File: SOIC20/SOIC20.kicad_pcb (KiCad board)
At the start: 2 copper layers, 20.6 x 25.7 mm, 8 parts, among them J1 Conn_01x10, J2 Conn_02x10_Counter_Clockwise, J3 Conn_02x10_Counter_Clockwise, J4 Conn_02x10_Counter_Clockwise, J5 Conn_01x10

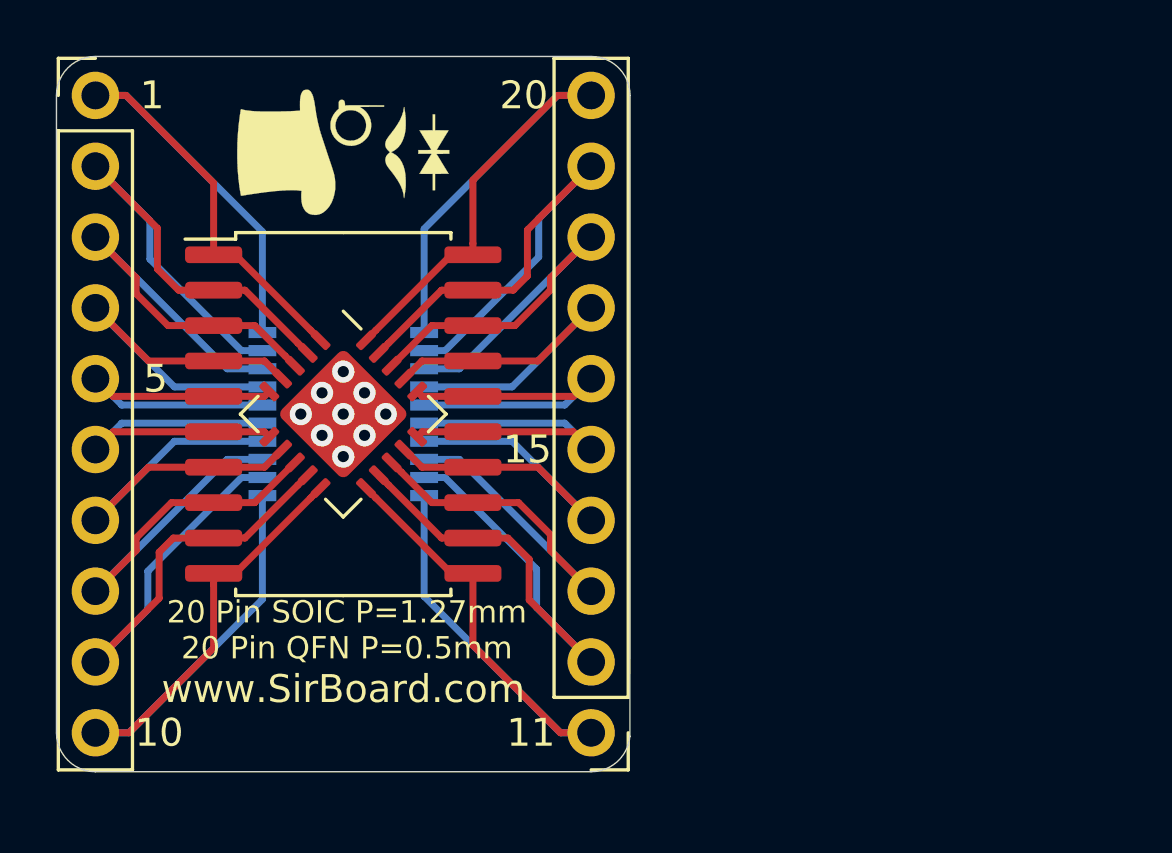
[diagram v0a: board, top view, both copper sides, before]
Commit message: Silkscreens and sizes updated
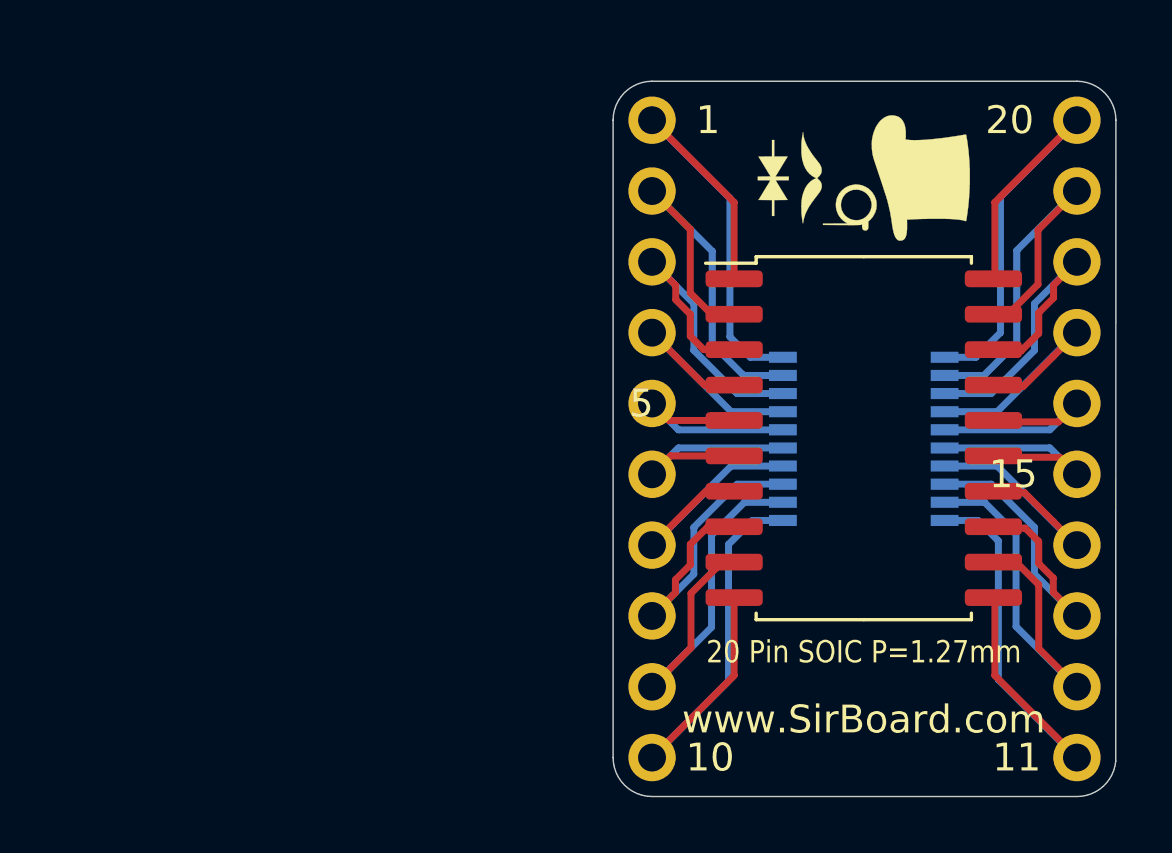
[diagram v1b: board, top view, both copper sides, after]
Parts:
- removed J3: Conn_02x10_Counter_Clockwise, Package_DFN_QFN:QFN-20-1EP_5x5mm_P0.65mm_EP3.35x3.35mm
- moved J1 20.0 mm to (154.6, 105.0)
- moved G*** 18.7 mm to (162.2, 107.1), turned to 270 degrees
- moved G*** 18.7 mm to (162.2, 124.9)
- moved J4 18.7 mm to (162.2, 116.5)
- moved G*** 18.7 mm to (162.2, 109.2)
- moved J2 18.7 mm to (162.2, 116.4)
- moved J5 17.4 mm to (169.8, 127.9)
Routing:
- net Net-(J2-Pad20): track 25.0 -> 18.0 mm
- net Net-(J1-Pad10): track 25.0 -> 18.0 mm
- net Net-(J2-Pad11): track 24.9 -> 18.0 mm
- net Net-(J1-Pad1): track 24.9 -> 18.0 mm
- net Net-(J1-Pad9): track 20.9 -> 15.3 mm
- net Net-(J2-Pad19): track 20.9 -> 15.3 mm
- net Net-(J1-Pad4): track 14.9 -> 9.59 mm
- net Net-(J2-Pad14): track 14.9 -> 9.59 mm
- net Net-(J2-Pad17): track 14.9 -> 9.61 mm
- net Net-(J1-Pad7): track 14.9 -> 9.61 mm
- net Net-(J1-Pad2): track 20.8 -> 15.5 mm
- net Net-(J2-Pad12): track 20.8 -> 15.5 mm
- net Net-(J2-Pad13): track 17.4 -> 12.6 mm
- net Net-(J1-Pad3): track 17.4 -> 12.6 mm
- net Net-(J1-Pad8): track 17.3 -> 12.6 mm
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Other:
- board size 20.6 x 25.7 mm -> 18 x 25.7 mm
- board text added: "20 Pin SOIC P=1.27mm"
- board text removed: "20 Pin SOIC P=1.27mm 20 Pin QFN P=0.5mm"

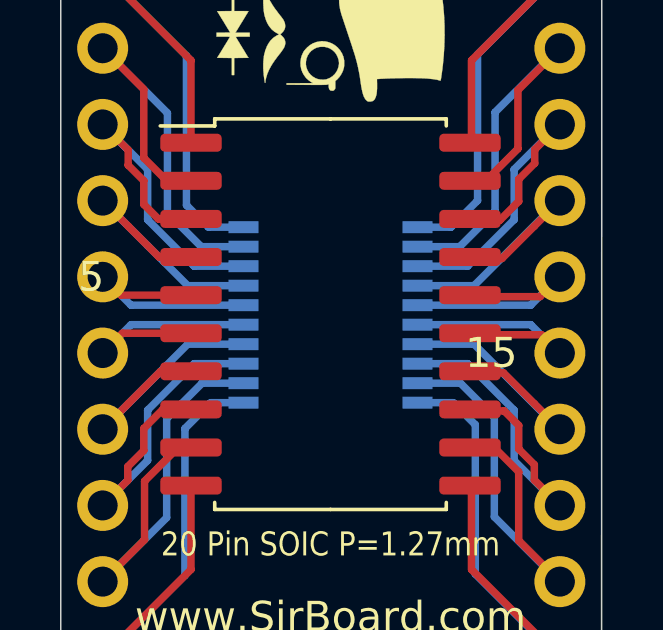
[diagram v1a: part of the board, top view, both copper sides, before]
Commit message: Dimensions Added And TQFP64 Added
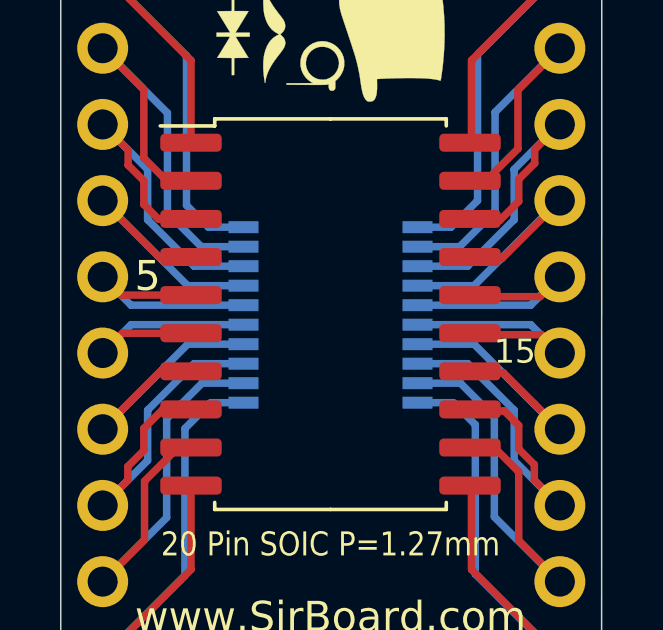
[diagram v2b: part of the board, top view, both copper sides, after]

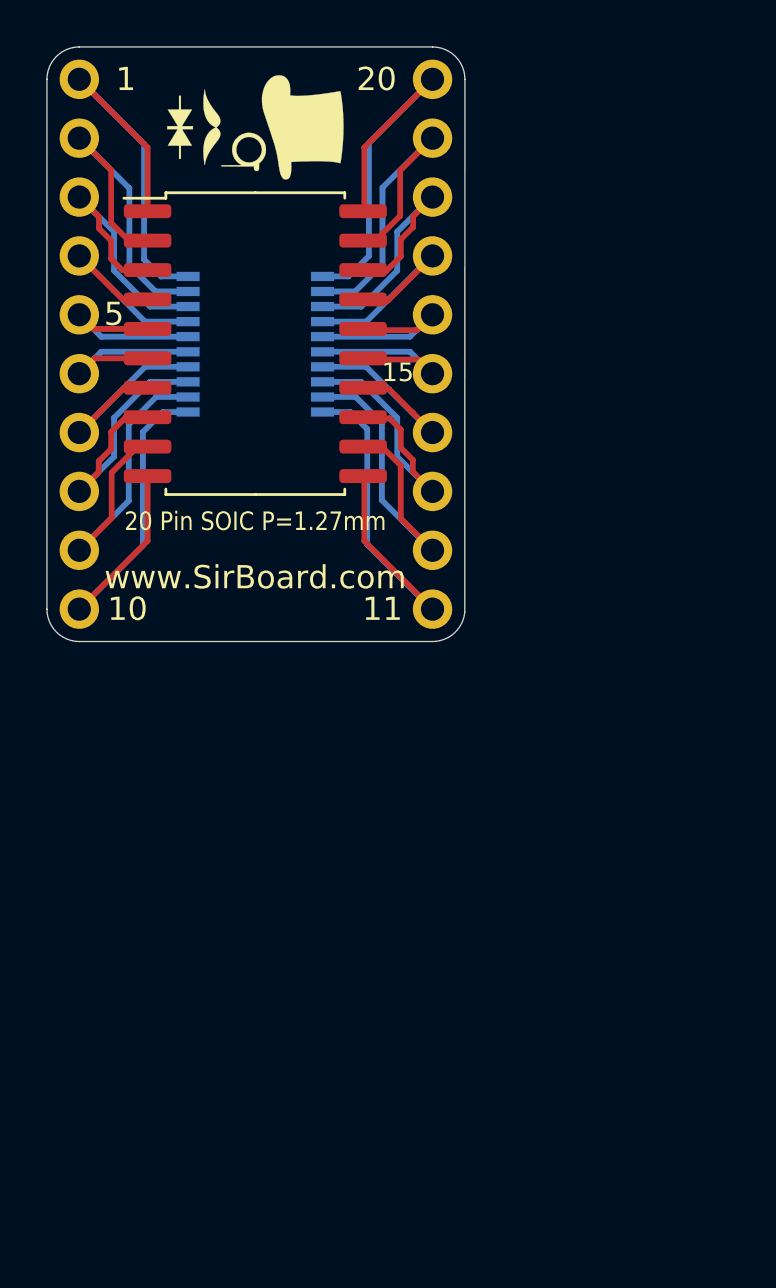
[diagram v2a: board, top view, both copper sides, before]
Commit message: Numbering Orientation Edited
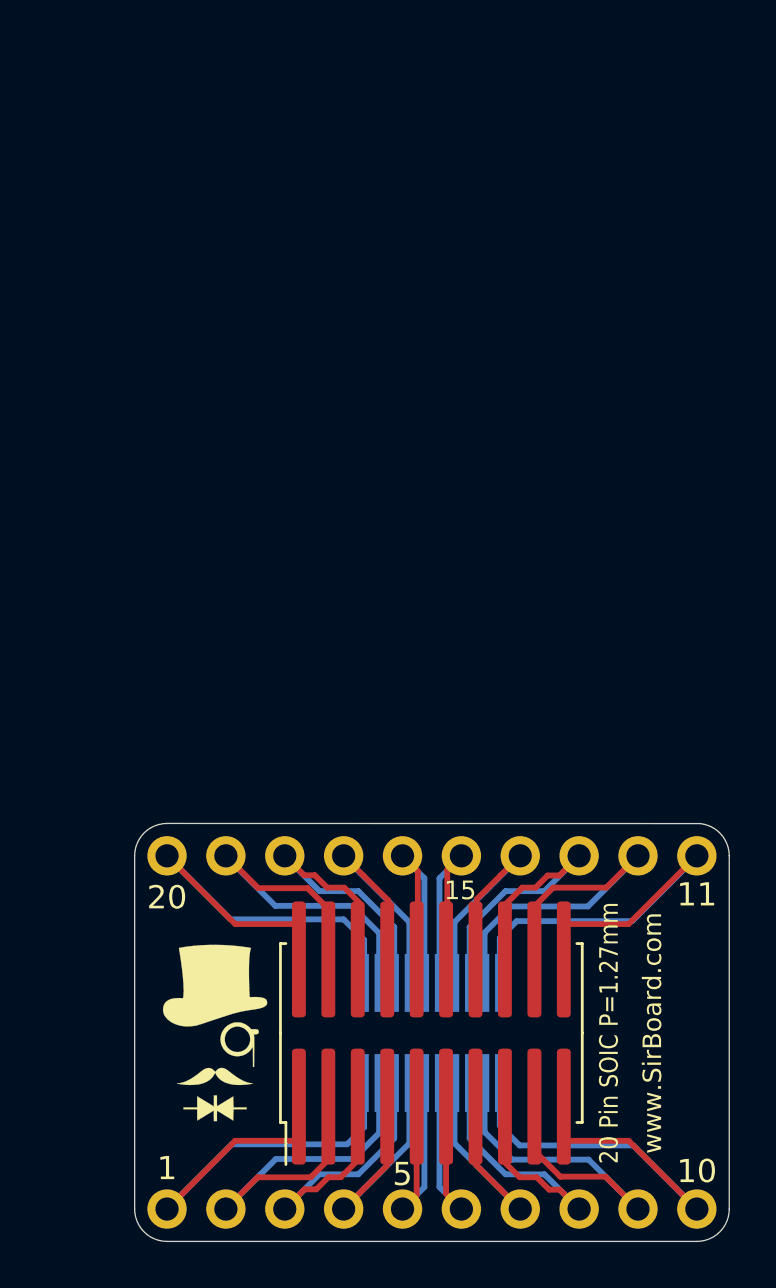
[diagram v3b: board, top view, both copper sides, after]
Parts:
- removed the G*** at (162.2, 124.9)
- added G***: LOGO, logo:logo94x134, B.Cu at (177.7, 146.3)
- J1, J5: moved to B.Cu
- moved J1 48.9 mm to (158.4, 153.8), turned to 270 degrees
- moved G*** 39.1 mm to (160.5, 146.2), turned to 0 degrees
- moved G*** 37.0 mm to (162.5, 146.2), turned to 90 degrees
- moved J2 30.7 mm to (169.8, 146.2), turned to 90 degrees
- moved J4 30.7 mm to (169.8, 146.2), turned to 90 degrees
- moved J5 15.6 mm to (181.2, 138.5), turned to 90 degrees
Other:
- board size 18 x 25.7 mm -> 25.7 x 18 mm

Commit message: Silkscreen Edits
Dimensions moved to Drawings Layer
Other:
- rule pad_to_mask_clearance: 0.051 -> 0
- rule solder_mask_min_width: 0.25 -> 0.1
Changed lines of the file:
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@@
   (general
     (thickness 1.6)
-    (drawings 35)
+    (drawings 28)
     (tracks 134)
     (zones 0)
@@
     (36 B.SilkS user)
     (37 F.SilkS user)
-    (38 B.Mask user hide)
-    (39 F.Mask user hide)
+    (38 B.Mask user)
+    (39 F.Mask user)
     (40 Dwgs.User user)
     (41 Cmts.User user hide)
@@
     (pad_size 1.7 1.7)
     (pad_drill 1)
-    (pad_to_mask_clearance 0.051)
-    (solder_mask_min_width 0.25)
+    (pad_to_mask_clearance 0)
+    (solder_mask_min_width 0.1)
     (aux_axis_origin 0 0)
     (visible_elements 7FFFFFFF)
     (pcbplotparams
-      (layerselection 0x010fc_ffffffff)
+      (layerselection 0x010f0_ffffffff)
       (usegerberextensions false)
       (usegerberattributes false)
@@
       (viasonmask false)
       (mode 1)
-      (useauxorigin false)
+      (useauxorigin true)
       (hpglpennumber 1)
       (hpglpenspeed 20)
@@
       (psa4output false)
       (plotreference true)
-      (plotvalue true)
+      (plotvalue false)
       (plotinvisibletext false)
       (padsonsilk false)
@@
       (outputformat 1)
       (mirror false)
-      (drillshape 1)
+      (drillshape 0)
       (scaleselection 1)
-      (outputdirectory ""))
+      (outputdirectory "../../Gerbers/SOIC20/"))
   )
   (net 0 "")
@@
       (xy -0.06096 3.169456) (xy -0.06096 2.6924) (xy 0.07112 2.6924) (xy 0.07112 2.926926)) (layer F.SilkS) (width 0.01))
   )
-  (dimension 18.034 (width 0.15) (layer F.SilkS)
-    (gr_text "18.034 mm" (at 188.625 146.1516 90) (layer F.SilkS)
+  (dimension 18.034 (width 0.15) (layer Dwgs.User)
+    (gr_text "18.034 mm" (at 188.625 146.1516 90) (layer Dwgs.User)
       (effects (font (size 1 1) (thickness 0.15)) hide)
     )
@@
     (arrow2b (pts (xy 187.325 155.1686) (xy 186.738579 154.042096)))
   )
-  (dimension 15.24 (width 0.12) (layer F.SilkS)
-    (gr_text "15.240 mm" (at 185.801 146.1516 90) (layer F.SilkS)
+  (dimension 15.24 (width 0.12) (layer Dwgs.User)
+    (gr_text "15.240 mm" (at 185.801 146.1516 90) (layer Dwgs.User)
       (effects (font (size 1 1) (thickness 0.15)) hide)
     )
@@
     (effects (font (size 1 1) (thickness 0.15)))
   )
-  (dimension 25.587 (width 0.12) (layer F.SilkS)
-    (gr_text "25.587 mm" (at 169.7655 131.064) (layer F.SilkS)
+  (dimension 25.587 (width 0.12) (layer Dwgs.User)
+    (gr_text "25.587 mm" (at 169.7655 131.064) (layer Dwgs.User)
       (effects (font (size 1 1) (thickness 0.15)) hide)
     )
@@
     (arrow2b (pts (xy 156.972 132.334) (xy 158.098504 131.747579)))
   )
-  (dimension 22.86 (width 0.12) (layer F.SilkS)
-    (gr_text "22.860 mm" (at 169.799 134.112) (layer F.SilkS)
+  (dimension 22.86 (width 0.12) (layer Dwgs.User)
+    (gr_text "22.860 mm" (at 169.799 134.112) (layer Dwgs.User)
       (effects (font (size 1 1) (thickness 0.15)) hide)
     )
@@
   (gr_arc (start 158.369 153.7716) (end 156.972 153.7716) (angle -90) (layer Edge.Cuts) (width 0.05))
   (gr_arc (start 158.369 138.5316) (end 158.369 137.1346) (angle -90) (layer Edge.Cuts) (width 0.05))
-  (gr_circle (center 144.267092 114.808) (end 144.566984 114.808) (layer B.Mask) (width 0.2))
-  (gr_circle (center 145.038908 115.57) (end 145.3388 115.57) (layer B.Mask) (width 0.2))
-  (gr_circle (center 143.505092 115.57) (end 143.804984 115.57) (layer B.Mask) (width 0.2))
-  (gr_circle (center 144.276908 116.332) (end 144.5768 116.332) (layer B.Mask) (width 0.2))
-  (gr_circle (center 143.514908 117.094) (end 143.8148 117.094) (layer B.Mask) (width 0.2))
-  (gr_circle (center 142.752908 116.332) (end 143.0528 116.332) (layer B.Mask) (width 0.2))
-  (gr_circle (center 141.986 115.574908) (end 142.285892 115.574908) (layer B.Mask) (width 0.2))
   (segment (start 178.2844 150.827) (end 181.229 153.7716) (width 0.25) (layer F.Cu) (net 1))
   (segment (start 175.4886 150.827) (end 178.2844 150.827) (width 0.25) (layer F.Cu) (net 1))

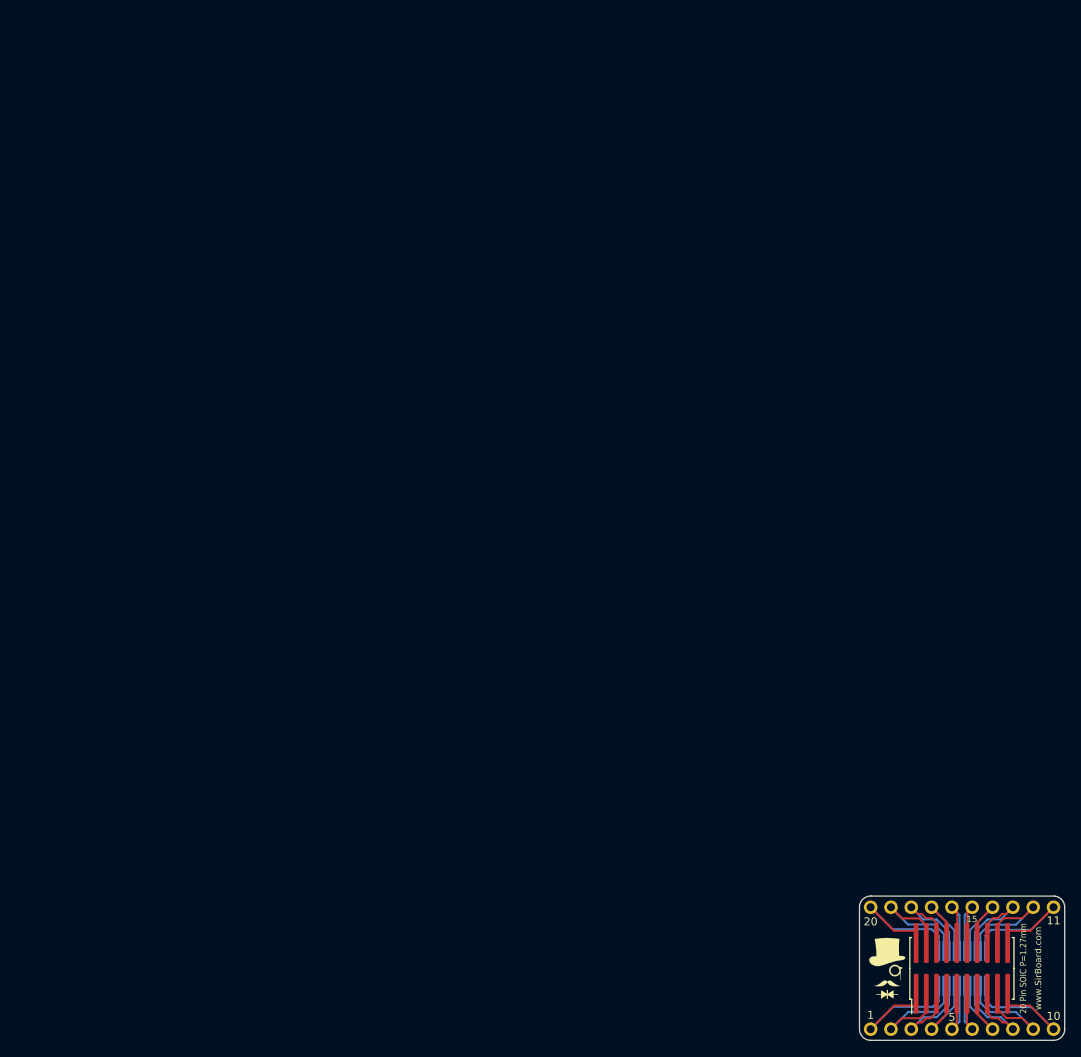
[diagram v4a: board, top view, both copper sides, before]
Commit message: USB, SD and CR Cells Added
MicroSD, MicroUSB, MiniUSB, USB-C, CR1220, CR2032 added as well as all schematics page sizes optimised
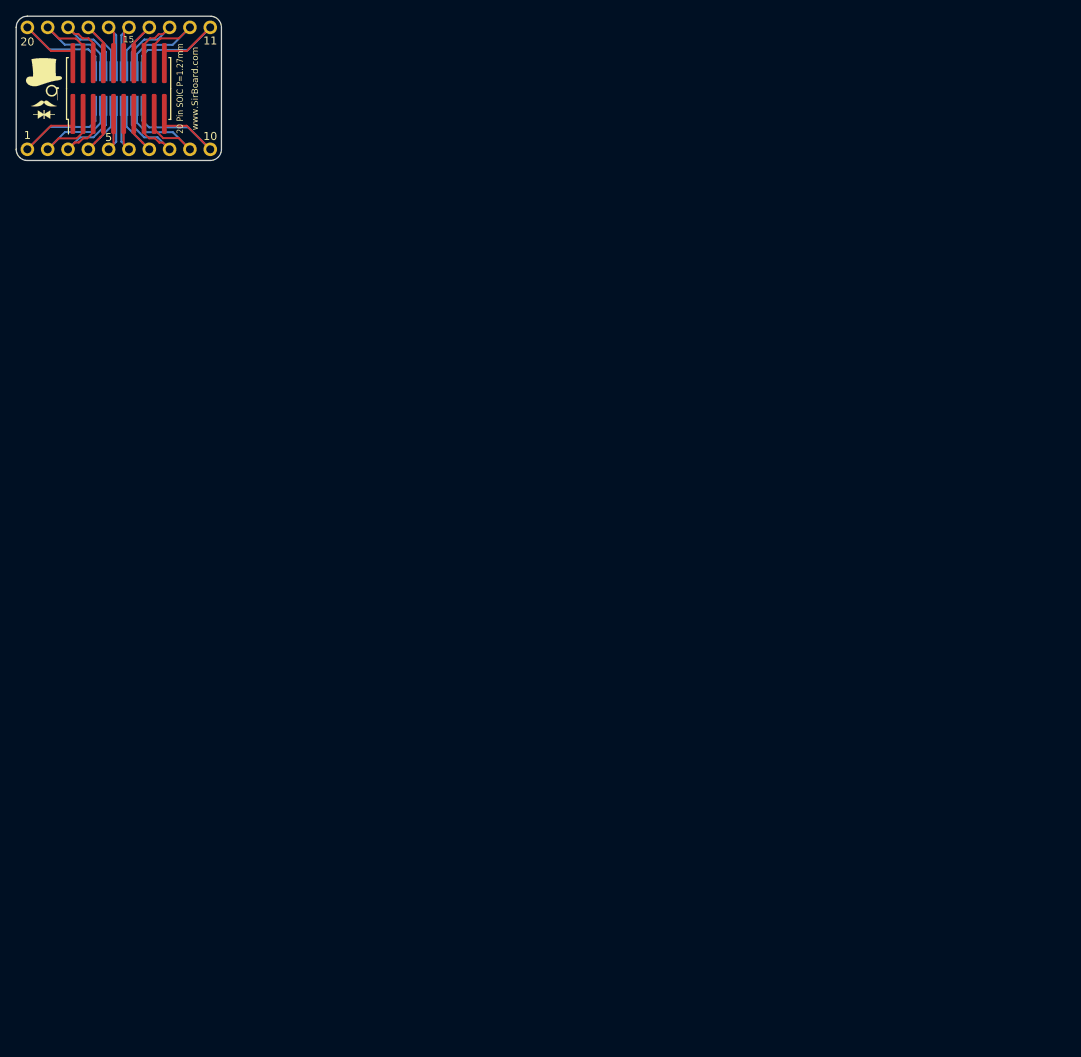
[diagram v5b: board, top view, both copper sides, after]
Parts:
- moved G*** 152.3 mm to (57.1, 36.2)
- moved J4 152.3 mm to (64.4, 36.2)
- moved J5 152.3 mm to (75.8, 28.5)
- moved G*** 152.3 mm to (72.3, 36.3)
- moved G*** 152.3 mm to (55.0, 36.2)
- moved J1 152.3 mm to (53.0, 43.8)
- moved J2 152.3 mm to (64.4, 36.2)
